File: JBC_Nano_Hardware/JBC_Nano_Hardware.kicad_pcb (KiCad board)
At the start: 2 copper layers, 48 x 49 mm, 57 parts, among them J1 POWER_IN, J2 IRON, J3 PROG, J4 UART, J5 Display128x32, Q1 IRF8721PBF-1, SW1 Rotary_Encoder_Switch, SW2 RESET, SW3 BOOT, U1 STM32F030F4Px, U2 AP1117-33, U3 NCP1117-12_SOT223, U4 AD8615, U5 UCC2751, U6 AT24CS01-STUM, Y1 Crystal_GND24

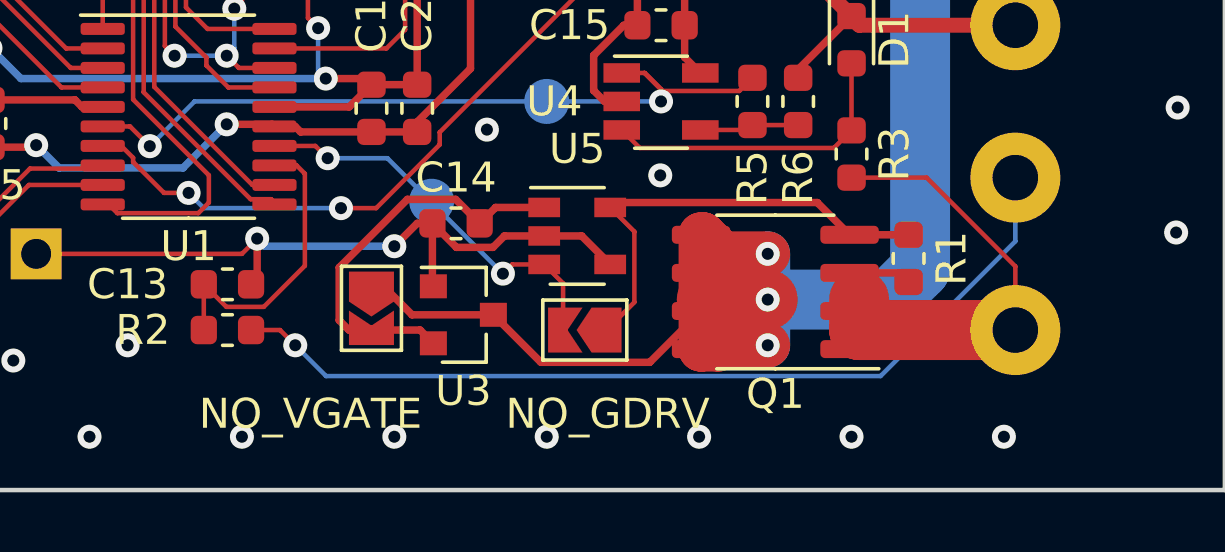
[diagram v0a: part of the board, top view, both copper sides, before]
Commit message: Fixed hardware issue (wrong mosfet)
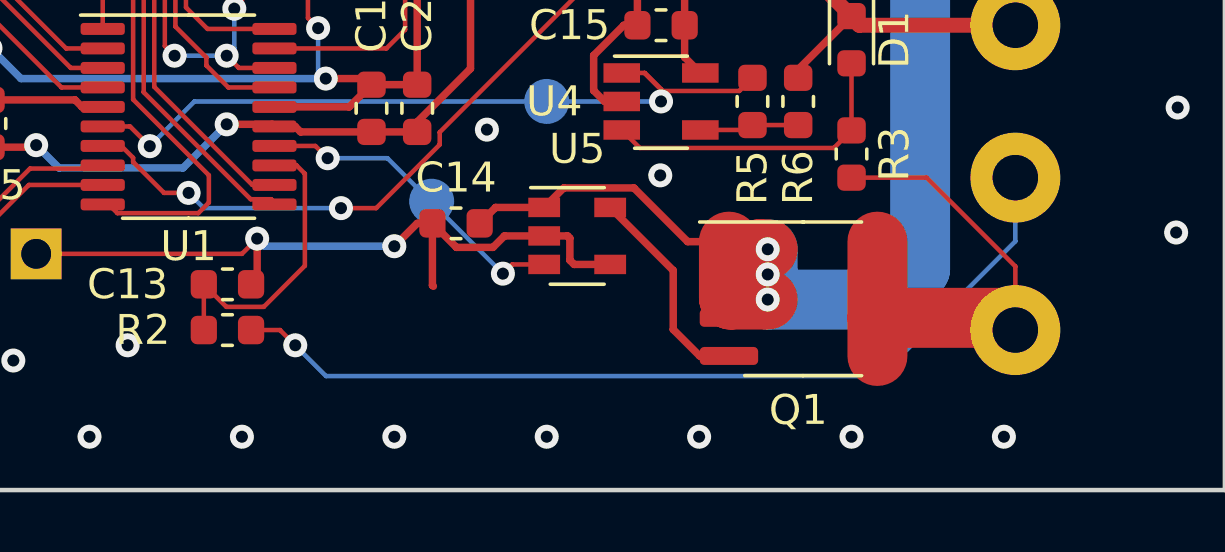
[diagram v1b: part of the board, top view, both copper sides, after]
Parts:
- removed JP1: NO_VGATE_REG, Jumper:SolderJumper-2_P1.3mm_Open_TrianglePad1.0x1.5mm
- removed JP2: NO_GATE_DRV, Jumper:SolderJumper-2_P1.3mm_Open_TrianglePad1.0x1.5mm
- removed R1: 1K, Resistor_SMD:R_0603_1608Metric
- removed U3: NCP1117-12_SOT223, Package_TO_SOT_SMD:SOT-23
- Q1: value IRF8721PBF-1 -> FDS9435A
- moved Q1 0.96 mm to (56.8, 65.3), turned to 0 degrees
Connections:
- C14 pad 1: Net-(C14-Pad1) -> VDC
- Q1 pad 1: Net-(J2-Pad4) -> VDC
- Q1 pad 2: Net-(J2-Pad4) -> VDC
- Q1 pad 3: Net-(J2-Pad4) -> VDC
- Q1 pad 5: VDC -> Net-(J2-Pad4)
- Q1 pad 6: VDC -> Net-(J2-Pad4)
- Q1 pad 7: VDC -> Net-(J2-Pad4)
- Q1 pad 8: VDC -> Net-(J2-Pad4)
- U5 pad 1: Net-(C14-Pad1) -> VDC
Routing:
- net VDC: track 101.5 -> 85.3 mm
- net Net-(C14-Pad1): track 13.5 -> 0.00 mm
- net /HEATER_GATE: track 15.3 -> 7.16 mm
- net /HEATER_ON: track 13.3 -> 10.9 mm
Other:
- board text removed: "NO_GDRV"
- board text removed: "NO_VGATE"

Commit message: Cleaned schematic and updated to KiCad 6
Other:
- net class Default removed
